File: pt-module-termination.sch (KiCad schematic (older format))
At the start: 2 parts

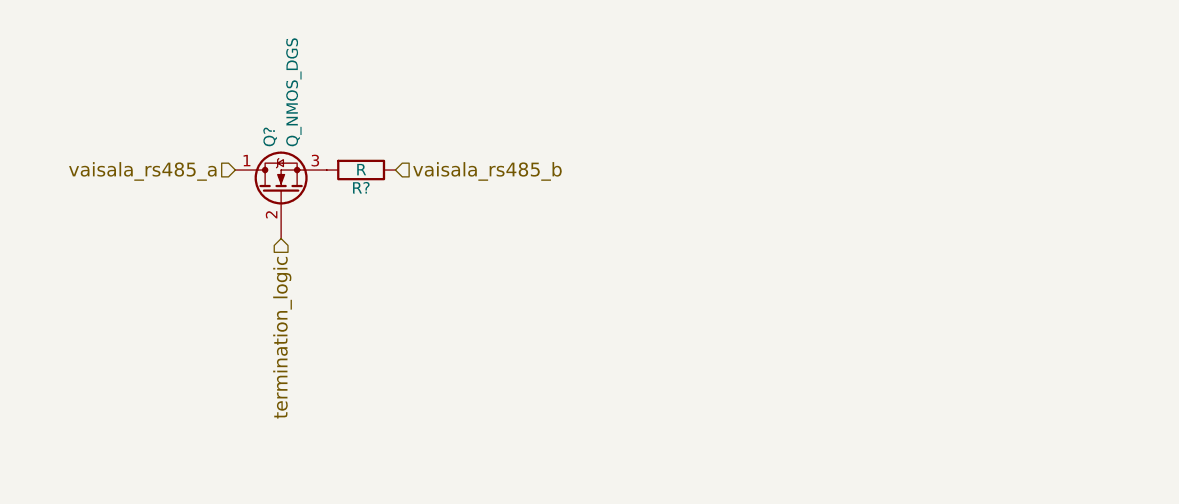
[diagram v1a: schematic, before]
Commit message: add termination switch
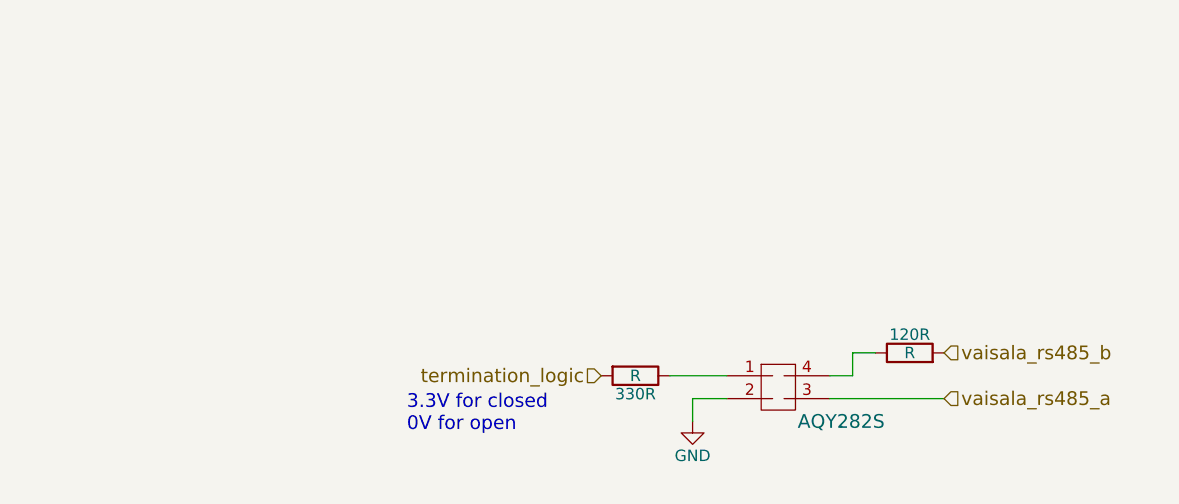
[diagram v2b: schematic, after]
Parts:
- removed Q?: Q_NMOS_DGS, symbol Q_NMOS_DGS
- added .: AQY282S, symbol AQY282S
- added 330R: R, symbol R
- gave numbers to parts that had none: 1
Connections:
- net termination_logic: now also 330R.2
- net vaisala_rs485_a: now also ..3
- net vaisala_rs485_b: now also 120R.2; no longer 120R.1
- new net: ..4, 120R.1
- new net: ..1, 330R.1
- new net GND: ..2
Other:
- note added: "3.3V for closed\n0V for open"
- moved on the sheet: 120R
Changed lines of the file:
@@
 $Descr A4 11693 8268
 encoding utf-8
-Sheet 7 12
+Sheet 6 13
 Title ""
 Date ""
@@
 Comment4 ""
 $EndDescr
-Text HLabel 3200 2350 0    60   Input ~ 0
+Text HLabel 6300 3350 2    60   Input ~ 0
 vaisala_rs485_a
-Text HLabel 3900 2350 2    60   Input ~ 0
+Text HLabel 6300 3150 2    60   Input ~ 0
 vaisala_rs485_b
 $Comp
-L Q_NMOS_DGS Q?
-U 1 1 5987C0B5
-P 3400 2450
-F 0 "Q?" H 3600 2500 50  0000 L CNN
-F 1 "Q_NMOS_DGS" H 3600 2400 50  0000 L CNN
-F 2 "" H 3600 2550 50  0001 C CNN
-F 3 "" H 3400 2450 50  0001 C CNN
-	1    3400 2450
+L R 120R
+U 1 1 5987C0FF
+P 6150 3150
+F 0 "120R" V 6230 3150 50  0000 C CNN
+F 1 "R" V 6150 3150 50  0000 C CNN
+F 2 "" V 6080 3150 50  0001 C CNN
+F 3 "" H 6150 3150 50  0001 C CNN
+	1    6150 3150
 	0    -1   -1   0
 $EndComp
+Text HLabel 4800 3250 0    60   Input ~ 0
+termination_logic
 $Comp
-L R R?
-U 1 1 5987C0FF
-P 3750 2350
-F 0 "R?" V 3830 2350 50  0000 C CNN
-F 1 "R" V 3750 2350 50  0000 C CNN
-F 2 "" V 3680 2350 50  0001 C CNN
-F 3 "" H 3750 2350 50  0001 C CNN
-	1    3750 2350
+L AQY282S .
+U 1 1 598B2987
+P 5850 3450
+F 0 "." H 5850 3450 60  0000 C CNN
+F 1 "AQY282S" H 5850 3450 60  0000 C CNN
+F 2 "" H 5850 3450 60  0001 C CNN
+F 3 "" H 5850 3450 60  0001 C CNN
+	1    5850 3450
+	1    0    0    -1
+$EndComp
+$Comp
+L GND #PWR?
+U 1 1 598B2D7C
+P 5200 3450
+F 0 "#PWR?" H 5200 3200 50  0001 C CNN
+F 1 "GND" H 5200 3300 50  0000 C CNN
+F 2 "" H 5200 3450 50  0001 C CNN
+F 3 "" H 5200 3450 50  0001 C CNN
+	1    5200 3450
+	1    0    0    -1
+$EndComp
+$Comp
+L R 330R
+U 1 1 598B2DEE
+P 4950 3250
+F 0 "330R" V 5030 3250 50  0000 C CNN
+F 1 "R" V 4950 3250 50  0000 C CNN
+F 2 "" V 4880 3250 50  0001 C CNN
+F 3 "" H 4950 3250 50  0001 C CNN
+	1    4950 3250
 	0    1    1    0
 $EndComp
-Text HLabel 3400 2650 3    60   Input ~ 0
-termination_logic
+Wire Wire Line
+	5350 3350 5200 3350
+Wire Wire Line
+	5200 3350 5200 3450
+Wire Wire Line
+	5350 3250 5100 3250
+Text Notes 3950 3500 0    60   ~ 0
+3.3V for closed\n0V for open
+Wire Wire Line
+	6000 3150 5900 3150
+Wire Wire Line
+	5900 3150 5900 3250
+Wire Wire Line
+	5900 3250 5800 3250
+Wire Wire Line
+	6300 3350 5800 3350
 $EndSCHEMATC

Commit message: Connected EVERYTHING. Ran ERC. There are still some power errors.
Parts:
- renumbered . to .1, 120R to 120R1, 330R to 330R1
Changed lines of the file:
@@
 LIBS:ftdi
 LIBS:relays
+LIBS:microchip_dspic33dsc
+LIBS:microchip_pic10mcu
+LIBS:microchip_pic12mcu
+LIBS:microchip_pic16mcu
+LIBS:microchip_pic18mcu
+LIBS:microchip_pic24mcu
+LIBS:microchip_pic32mcu
 LIBS:pt-module-cache
 EELAYER 25 0
@@
 vaisala_rs485_b
 $Comp
-L R 120R
+L R 120R1
 U 1 1 5987C0FF
 P 6150 3150
-F 0 "120R" V 6230 3150 50  0000 C CNN
+F 0 "120R1" V 6230 3150 50  0000 C CNN
 F 1 "R" V 6150 3150 50  0000 C CNN
 F 2 "" V 6080 3150 50  0001 C CNN
@@
 termination_logic
 $Comp
-L AQY282S .
+L AQY282S .1
 U 1 1 598B2987
 P 5850 3450
-F 0 "." H 5850 3450 60  0000 C CNN
+F 0 ".1" H 5850 3450 60  0000 C CNN
 F 1 "AQY282S" H 5850 3450 60  0000 C CNN
 F 2 "" H 5850 3450 60  0001 C CNN
@@
 $EndComp
 $Comp
-L GND #PWR?
+L GND #PWR061
 U 1 1 598B2D7C
 P 5200 3450
-F 0 "#PWR?" H 5200 3200 50  0001 C CNN
+F 0 "#PWR061" H 5200 3200 50  0001 C CNN
 F 1 "GND" H 5200 3300 50  0000 C CNN
 F 2 "" H 5200 3450 50  0001 C CNN
@@
 $EndComp
 $Comp
-L R 330R
+L R 330R1
 U 1 1 598B2DEE
 P 4950 3250
-F 0 "330R" V 5030 3250 50  0000 C CNN
+F 0 "330R1" V 5030 3250 50  0000 C CNN
 F 1 "R" V 4950 3250 50  0000 C CNN
 F 2 "" V 4880 3250 50  0001 C CNN

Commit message: add all the rest of the footprints
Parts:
- .1: footprint (none) -> Housings_DIP:DIP-8_W11.48mm_SMD
- 120R1: footprint (none) -> Resistors_THT:R_Axial_DIN0207_L6.3mm_D2.5mm_P7.62mm_Horizontal
- 330R1: footprint (none) -> Resistors_SMD:R_1206_HandSoldering
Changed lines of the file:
@@
 F 0 "120R1" V 6230 3150 50  0000 C CNN
 F 1 "R" V 6150 3150 50  0000 C CNN
-F 2 "" V 6080 3150 50  0001 C CNN
+F 2 "Resistors_THT:R_Axial_DIN0207_L6.3mm_D2.5mm_P7.62mm_Horizontal" V 6080 3150 50  0001 C CNN
 F 3 "" H 6150 3150 50  0001 C CNN
 	1    6150 3150
@@
 F 0 ".1" H 5850 3450 60  0000 C CNN
 F 1 "AQY282S" H 5850 3450 60  0000 C CNN
-F 2 "" H 5850 3450 60  0001 C CNN
+F 2 "Housings_DIP:DIP-8_W11.48mm_SMD" H 5850 3450 60  0001 C CNN
 F 3 "" H 5850 3450 60  0001 C CNN
 	1    5850 3450
@@
 F 0 "330R1" V 5030 3250 50  0000 C CNN
 F 1 "R" V 4950 3250 50  0000 C CNN
-F 2 "" V 4880 3250 50  0001 C CNN
+F 2 "Resistors_SMD:R_1206_HandSoldering" V 4880 3250 50  0001 C CNN
 F 3 "" H 4950 3250 50  0001 C CNN
 	1    4950 3250
